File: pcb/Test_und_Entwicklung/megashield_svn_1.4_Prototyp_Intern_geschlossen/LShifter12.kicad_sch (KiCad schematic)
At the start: 3 parts, among them Q34 BSS138 (2n7002)

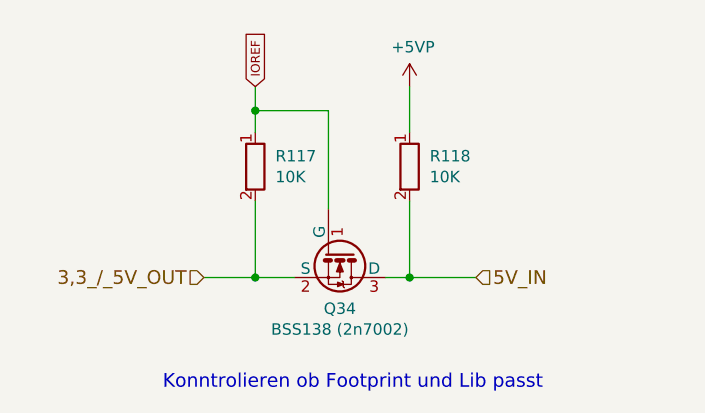
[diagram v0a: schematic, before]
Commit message: megashield_svn_1.4_Prototyp_Intern_geschlossen
megashield_svn_1.4_Prototyp_Intern_geschlossen
3D Kicad Symbolpfade angepasst
Anmerkungen in Schaltplan zu den Änderungen der 1.4 Platine entfernt
Schaltplan als PDF erstellt
Datei Leichen in Archiv verschoben
Unterordner für Datenblättererstellt
Unterordner für Produktionsdaten erstellt
Schaltplan und Platinen Layout Kicad Format geändert (von Kicad automatisch geändert)
+ Am Schaltplan und dem Platinen Layout wurden keine Änderungen vorgenommen+
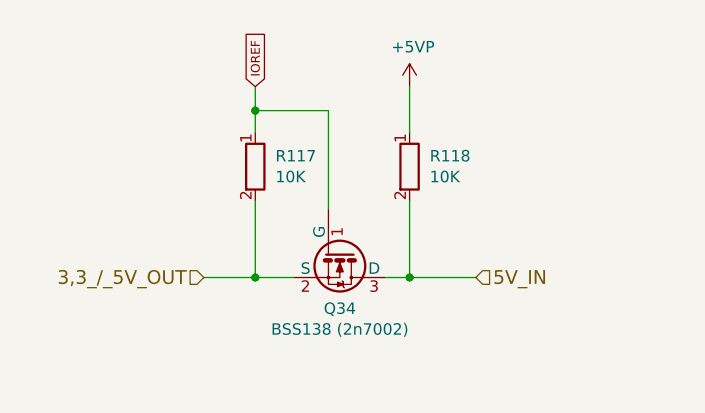
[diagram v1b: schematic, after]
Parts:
- Q34: Bestücken (Assemble) JA (YES) -> (none); Funktion Transistor SMD N-FET SOT-23 50 V 0.22 A -> (none); JLCPCB LCSC Part C8545 -> (none); Reichelt-Bestellnummer R: BSS 138 SMD -> (none)
- R117, R118: Funktion SMD-Widerstand, 0603, 10 kOhm, 100 mW, 1% -> (none); Hersteller Value -> (none); Hersteller Bestellnummer Value -> (none); Reichelt-Bestellnummer R: RND 0603 1 10K -> (none)
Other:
- note removed: "Konntrolieren ob Footprint und Lib passt"
